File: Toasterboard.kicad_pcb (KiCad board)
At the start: 2 copper layers, 2 parts, among them U1 LM341T-05_TO220, U2 NE555P

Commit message: feat: finished basic logics
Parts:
- added C1: 0.01uF, PCM_Capacitor_THT_US_AKL:C_Disc_D5.0mm_W2.5mm_P5.00mm, F.Cu at (129.0, 88.5)
- added C2: 100uF, PCM_Capacitor_THT_US_AKL:CP_Radial_D5.0mm_P2.00mm, F.Cu at (120.5, 79.0)
- added C3: 100uF, PCM_Capacitor_THT_US_AKL:CP_Radial_D5.0mm_P2.00mm, F.Cu at (120.5, 88.5)
- added J1: Power, Connector_PinHeader_2.54mm:PinHeader_1x04_P2.54mm_Vertical, B.Cu at (96.5, 71.0)
- added J2: LEDs, Connector_PinHeader_2.54mm:PinHeader_1x04_P2.54mm_Vertical, B.Cu at (118.4, 71.0)
- added J3: Switches, Connector_PinHeader_2.54mm:PinHeader_1x04_P2.54mm_Vertical, B.Cu at (133.5, 71.0)
- added LED1: Red, LED_THT:LED_D3.0mm, F.Cu at (140.7, 77.5)
- added LED2: Red, LED_THT:LED_D3.0mm, F.Cu at (140.7, 83.5)
- added LED3: Red, LED_THT:LED_D3.0mm, F.Cu at (140.7, 89.5)
- added LED4: Red, LED_THT:LED_D3.0mm, F.Cu at (140.8, 95.5)
- added LED_CLK1: Green, LED_THT:LED_D3.0mm, F.Cu at (103.0, 78.5)
- added RV1: 10k, Potentiometer_THT:Potentiometer_Piher_PT-15-V02_Vertical, F.Cu at (150.1, 113.0)
- added R_CLK1: 1k, PCM_Resistor_THT_US_AKL:R_Axial_DIN0207_L6.3mm_D2.5mm_P5.08mm_Vertical, F.Cu at (110.2, 78.0)
- added R_LED1: 1k, PCM_Resistor_THT_US_AKL:R_Axial_DIN0207_L6.3mm_D2.5mm_P5.08mm_Vertical, F.Cu at (146.7, 77.5)
- added R_LED2: 1k, PCM_Resistor_THT_US_AKL:R_Axial_DIN0207_L6.3mm_D2.5mm_P5.08mm_Vertical, F.Cu at (146.9, 83.5)
- added R_LED3: 1k, PCM_Resistor_THT_US_AKL:R_Axial_DIN0207_L6.3mm_D2.5mm_P5.08mm_Vertical, F.Cu at (146.9, 89.5)
- added R_LED4: 1k, PCM_Resistor_THT_US_AKL:R_Axial_DIN0207_L6.3mm_D2.5mm_P5.08mm_Vertical, F.Cu at (146.7, 95.5)
- added R_RV1: 1k, PCM_Resistor_THT_US_AKL:R_Axial_DIN0207_L6.3mm_D2.5mm_P5.08mm_Vertical, F.Cu at (129.2, 79.0)
- added SW1: SW_SPDT, Button_Switch_THT:SW_Slide_SPDT_Straight_CK_OS102011MS2Q, F.Cu at (158.0, 77.5)
- added SW2: SW_SPDT, Button_Switch_THT:SW_Slide_SPDT_Straight_CK_OS102011MS2Q, F.Cu at (158.0, 83.5)
- added SW3: SW_SPDT, Button_Switch_THT:SW_Slide_SPDT_Straight_CK_OS102011MS2Q, F.Cu at (158.0, 89.5)
- added SW4: SW_SPDT, Button_Switch_THT:SW_Slide_SPDT_Straight_CK_OS102011MS2Q, F.Cu at (158.0, 95.5)
- added U3: 74LS14, Package_DIP:DIP-14_W7.62mm_Socket, F.Cu at (118.9, 103.3)
- U1: footprint Package_TO_SOT_THT:TO-220-3_Vertical -> Package_TO_SOT_THT:TO-220-3_Horizontal_TabDown
- U2: footprint Package_DIP:DIP-8_W7.62mm -> Package_DIP:DIP-8_W7.62mm_Socket
- moved U1 66.3 mm to (92.9, 93.0)
- moved U2 29.8 mm to (104.5, 91.6), turned to 90 degrees
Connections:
- U2 pad 2: unconnected-(U2-TRIG-Pad2) -> Net-(U2-THRES)
- U2 pad 4: unconnected-(U2-~{RST}-Pad4) -> +5V
- U2 pad 6: unconnected-(U2-THRES-Pad6) -> Net-(U2-THRES)
- U2 pad 7: unconnected-(U2-DISCH-Pad7) -> Net-(U2-DISCH)
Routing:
- net GND: track 0.00 -> 176.9 mm
- net Net-(U2-DISCH): track 0.00 -> 135.9 mm
- net +5V: track 0.00 -> 135.4 mm
- net /Clk: track 0.00 -> 104.4 mm
- net Net-(U2-THRES): track 0.00 -> 76.2 mm
- net Net-(J3-Pin_4): track 0.00 -> 49.8 mm
- net Net-(J3-Pin_3): track 0.00 -> 45.7 mm
- net Net-(J3-Pin_2): track 0.00 -> 41.6 mm
- net Net-(J2-Pin_4): track 0.00 -> 34.4 mm
- net Net-(J2-Pin_3): track 0.00 -> 32.2 mm
- net Net-(J3-Pin_1): track 0.00 -> 29.5 mm
- net Net-(J2-Pin_2): track 0.00 -> 29.5 mm
- net Net-(J2-Pin_1): track 0.00 -> 29.1 mm
- net +12V: track 0.00 -> 27.5 mm
- net Net-(LED_CLK1-K): track 0.00 -> 17.2 mm
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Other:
- board outline added: 77.5 x 48 mm

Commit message: feat: finish routing
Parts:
- removed U1: LM341T-05_TO220, Package_TO_SOT_THT:TO-220-3_Horizontal_TabDown
- added D_Jack: 1N5817, Diode_THT:D_DO-41_SOD81_P2.54mm_Vertical_CathodeUp, F.Cu at (126.0, 96.5)
- added D_USB: 1N5817, Diode_THT:D_DO-41_SOD81_P2.54mm_Vertical_CathodeUp, F.Cu at (126.5, 100.6)
- added J1: Barrel Jack, Connector_BarrelJack:BarrelJack_GCT_DCJ200-10-A_Horizontal, F.Cu at (117.5, 98.6)
- added LM341T: LM341T-05_TO220, Package_TO_SOT_THT:TO-220-3_Horizontal_TabDown, F.Cu at (109.3, 85.0)
- added RECT: CS10D, PCM_Diode_THT_AKL:Diode_Bridge_DIP-4_W7.62mm_P5.08mm, F.Cu at (138.4, 87.7)
- added REF**: PinHeader_1x32_P2.54mm_Vertical, Connector_PinHeader_2.54mm:PinHeader_1x32_P2.54mm_Vertical, F.Cu at (85.2, 63.5)
- added R_USB1: 5.1k, PCM_Resistor_THT_US_AKL:R_Axial_DIN0207_L6.3mm_D2.5mm_P2.54mm_Vertical, F.Cu at (132.0, 103.1)
- added R_USB2: 5.1k, PCM_Resistor_THT_US_AKL:R_Axial_DIN0207_L6.3mm_D2.5mm_P2.54mm_Vertical, F.Cu at (135.5, 103.1)
- added SW_PWR1: SW_SPDT, Button_Switch_THT:SW_Slide_SPDT_Straight_CK_OS102011MS2Q, F.Cu at (109.5, 102.5)
- added USB-C: USB_C_Plug_USB2.0, Connector_USB:USB_C_Receptacle_GCT_USB4135-GF-A_6P_TopMnt_Horizontal, F.Cu at (130.0, 109.0)
- 74HC14: renamed from U3; value 74LS14 -> 74HC14
- L CLK: renamed from LED_CLK1
- R_CLK1, R_LED1, R_LED2, R_LED3, R_LED4: footprint PCM_Resistor_THT_US_AKL:R_Axial_DIN0207_L6.3mm_D2.5mm_P5.08mm_Vertical -> PCM_Resistor_THT_US_AKL:R_Axial_DIN0207_L6.3mm_D2.5mm_P2.54mm_Vertical
- moved 555 37.9 mm to (139.3, 76.7), turned to -90 degrees
- moved C2 34.7 mm to (139.5, 108.0)
- moved J3 33.3 mm to (151.5, 67.5), turned to 90 degrees
- moved R_Pot 32.1 mm to (147.0, 105.7), turned to -90 degrees
- moved 74HC14 31.7 mm to (124.7, 72.2), turned to -90 degrees
- moved L CLK 31.3 mm to (133.8, 72.7), turned to 180 degrees
- moved J4 30.7 mm to (164.0, 67.5), turned to 90 degrees
- moved R_CLK1 27.7 mm to (137.2, 72.0)
- moved J2 27.1 mm to (123.4, 67.5)
- moved C1 22.8 mm to (147.0, 102.5), turned to 90 degrees
- moved C3 22.2 mm to (139.5, 100.0)
- moved L2 6.06 mm to (146.1, 80.7), turned to 180 degrees
- moved L1 6.04 mm to (146.1, 74.7), turned to 180 degrees
- moved L4 6.03 mm to (146.1, 92.7), turned to 180 degrees
- moved L3 6.02 mm to (146.1, 86.7), turned to 180 degrees
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- renumbered U2 to 555, J1 to J2, J2 to J3, J3 to J4, LED1 to L1, LED2 to L2, LED3 to L3, LED4 to L4, R_RV1 to R_Pot
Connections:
- 74HC14 pad 14: (no net) -> +5V
- 74HC14 pad 7: (no net) -> GND
- J2 pad 2: +12V -> +VDC
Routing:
- net GND: track 176.9 -> 40.1 mm, vias 0 -> 17
- net Net-(U2-DISCH): track 135.9 -> 30.9 mm
- net +5V: track 135.4 -> 210.5 mm
- net /Clk: track 104.4 -> 39.3 mm
- net +VDC: track 0.00 -> 62.0 mm
- net Net-(D_JACK1-A): track 0.00 -> 47.8 mm
- net +12V: track 27.5 -> 0.00 mm
- net Net-(D_USB1-A): track 0.00 -> 22.4 mm
- net Net-(D_RECT1-1): track 0.00 -> 22.4 mm
- net Net-(D_RECT1--): track 0.00 -> 21.6 mm
- net Net-(U2-THRES): track 76.2 -> 55.6 mm
- net Net-(J4-Pin_1): track 29.5 -> 9.37 mm
- net Net-(J4-Pin_2): track 41.6 -> 22.0 mm
- net Net-(J4-Pin_3): track 45.7 -> 26.5 mm
- net Net-(J3-Pin_1): track 29.1 -> 10.9 mm
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- added copper zone on B.Cu, net GND
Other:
- board size 77.5 x 48 mm -> 67 x 46.5 mm
- board text added: "Jack"
- board text added: "L1"
- board text added: "L2"
- board text added: "L3"
- board text added: "L4"
- board text added: "Mk. I"
- board text added: "Power Source"
- board text added: "R_USB"
- board text added: "S1"
- board text added: "S2"
- board text added: "S3"
- board text added: "S4"
- board text added: "SW2"
- board text added: "Toasterboard"
- board text added: "USB"

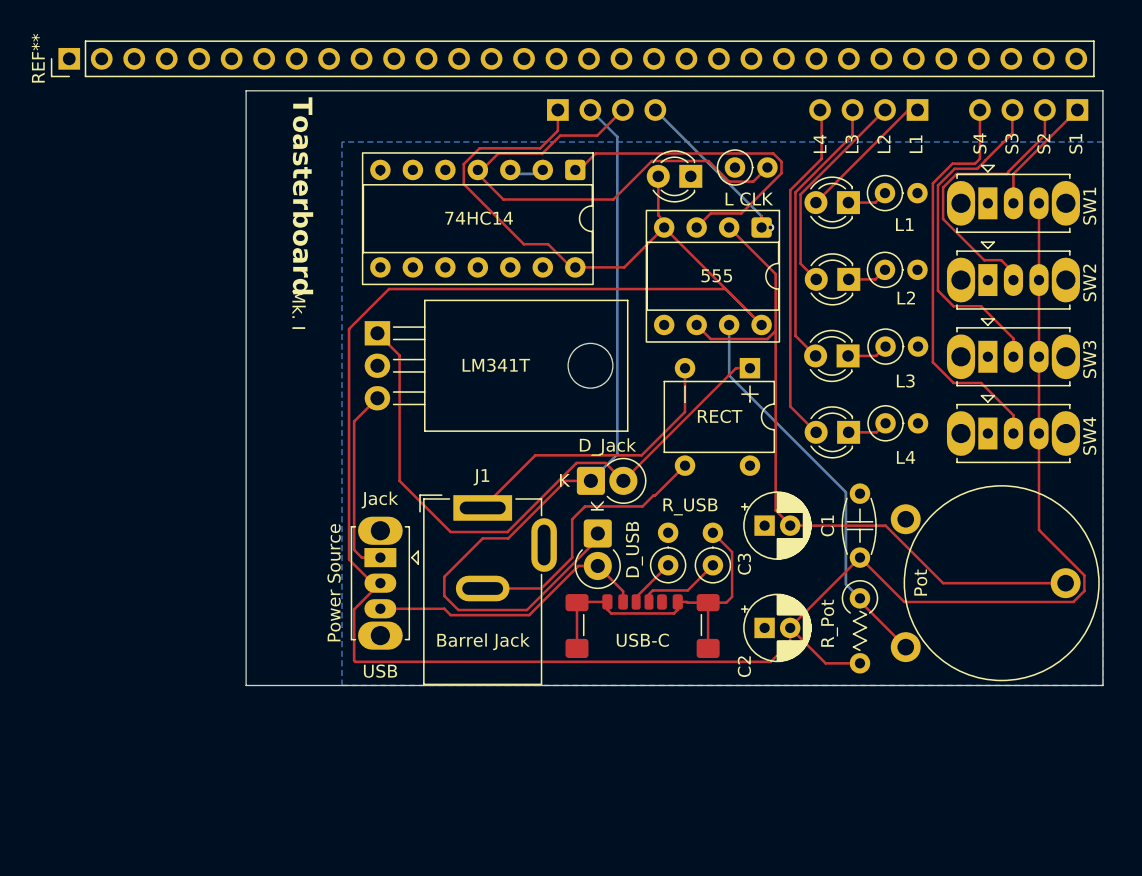
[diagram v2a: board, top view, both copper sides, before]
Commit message: feat: make board more compact, add branding
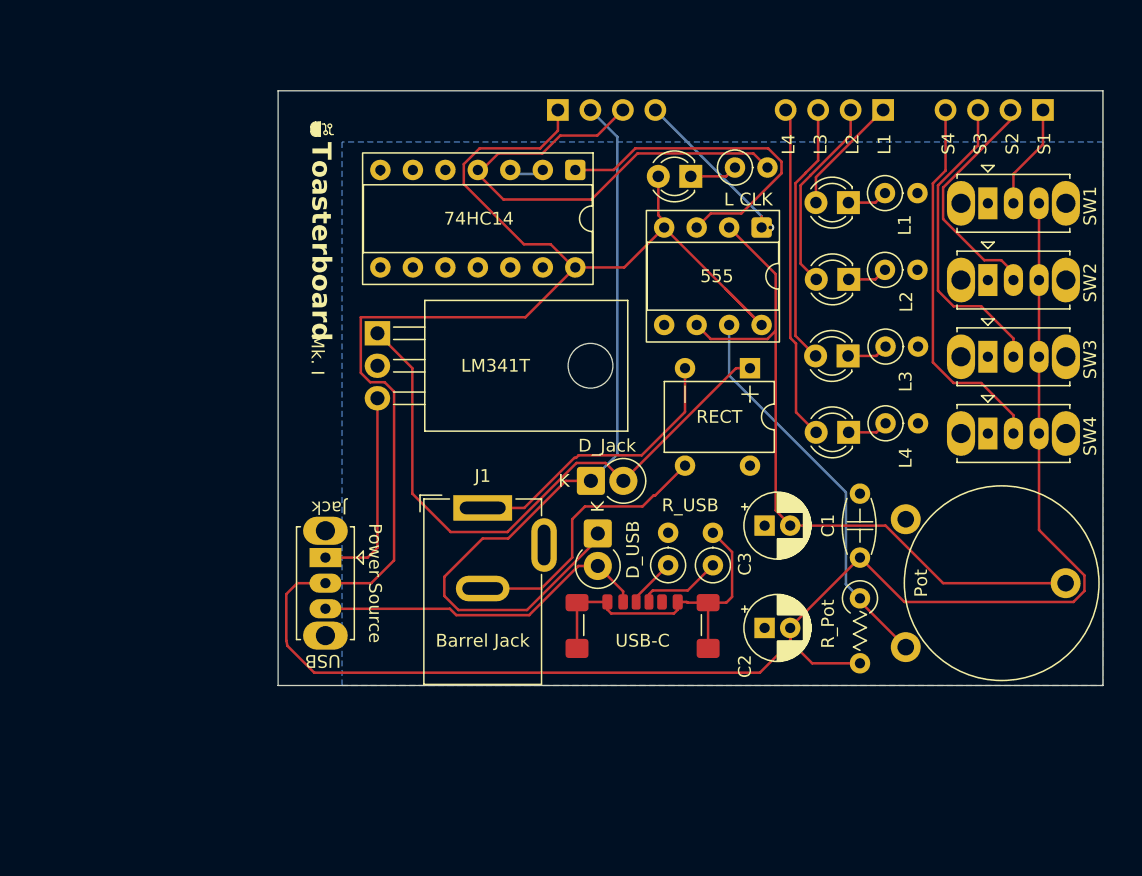
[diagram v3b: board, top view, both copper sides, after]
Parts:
- removed REF**: PinHeader_1x32_P2.54mm_Vertical, Connector_PinHeader_2.54mm:PinHeader_1x32_P2.54mm_Vertical
- moved SW_PWR1 4.30 mm to (105.2, 102.5)
- moved J3 2.69 mm to (148.8, 67.5)
- moved J4 2.69 mm to (161.3, 67.5)
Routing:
- net Net-(D_USB1-A): track 22.4 -> 27.4 mm
- net Net-(LED_CLK1-K): track 0.00 -> 3.74 mm
- net Net-(J4-Pin_2): track 22.0 -> 18.5 mm
- net Net-(J4-Pin_3): track 26.5 -> 24.3 mm
- net Net-(J4-Pin_4): track 31.7 -> 29.6 mm
- net Net-(SW_PWR1-A): track 14.9 -> 16.8 mm
- net Net-(J3-Pin_1): track 10.9 -> 9.42 mm
- net Net-(J3-Pin_2): track 16.5 -> 15.4 mm
- net Net-(J4-Pin_1): track 9.37 -> 8.25 mm
- net Net-(J3-Pin_3): track 21.7 -> 20.8 mm
- net Net-(J3-Pin_4): track 27.1 -> 26.2 mm
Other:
- board size 67 x 46.5 mm -> 64.5 x 46.5 mm
